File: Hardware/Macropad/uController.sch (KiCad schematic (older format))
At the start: 17 parts, among them J1 Conn_02x03_Odd_Even, SW11 SW_Push, U1 ATmega32U4-AU, X1 KC2016K

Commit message: Schematic mostly done. Started grouping components in layout
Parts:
- gave numbers to parts that had none: 3
- renumbered C13 to C32, C12 to C33, C14 to C34, C15 to C35, C16 to C36, J1 to J3, R6 to R17, R7 to R18, SW11 to SW22, U1 to U5
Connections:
- net USBD_N renamed DM1_N
- net USBD_P renamed DP1_P

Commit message: First pass of the layout done
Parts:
- removed R17: 4K7, resistor_smd:R_0603_1608Metric, symbol Device:R
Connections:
- net +3V3: now also X1.1 (EN)
- net COL[0]: now also U5.8 (PB0); no longer U5.1 (PE6)
- net COL[1]: now also U5.12 (PB7); no longer U5.40 (PF1)
- net COL[2]: now also U5.18 (PD0); no longer U5.41 (PF0)
- net COL[3]: now also U5.28 (PB4); no longer U5.27 (PD7)
- net RGB_OUT: now also U5.40 (PF1); no longer U5.18 (PD0)
- net ROT_ENC_A: now also U5.31 (PC6); no longer U5.29 (PB5)
- net ROT_ENC_B: now also U5.32 (PC7); no longer U5.30 (PB6)
- net ROW[0]: now also U5.25 (PD4); no longer U5.39 (PF4)
- net ROW[1]: now also U5.22 (PD5); no longer U5.38 (PF5)
- net ROW[2]: now also U5.21 (PD3); no longer U5.37 (PF6)
- net ROW[3]: now also U5.20 (PD2); no longer U5.36 (PF7)
- net ROW[4]: now also U5.19 (PD1); no longer U5.31 (PC6)
- net ROW[5]: now also U5.27 (PD7); no longer U5.32 (PC7)
- net SCL: now also U5.1 (PE6); no longer U5.20 (PD2)
- net SDA: now also U5.41 (PF0); no longer U5.19 (PD1)
- net DM1_N renamed USB_D4-
- net DP1_P renamed USB_D4+
- no-connect marks 5 -> 1
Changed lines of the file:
@@
 Wire Wire Line
 	5000 6250 5000 6300
-Text GLabel 5950 5500 2    50   Input ~ 0
+Text GLabel 5950 4500 2    50   Input ~ 0
 ROW[0]
-Text GLabel 5950 5600 2    50   Input ~ 0
+Text GLabel 5950 4600 2    50   Input ~ 0
 ROW[1]
-Text GLabel 5950 5700 2    50   Input ~ 0
+Text GLabel 5950 4400 2    50   Input ~ 0
 ROW[2]
-Text GLabel 5950 5400 2    50   Output ~ 0
-COL[1]
-Text GLabel 5950 5300 2    50   Output ~ 0
-COL[2]
-Wire Wire Line
-	5600 5700 5950 5700
-Wire Wire Line
-	5600 5500 5950 5500
-Wire Wire Line
-	5600 5300 5950 5300
-Wire Wire Line
-	5600 5400 5950 5400
+Wire Wire Line
+	5600 4400 5950 4400
+Wire Wire Line
+	5600 4500 5950 4500
+Wire Wire Line
+	5600 4100 5950 4100
 $Comp
 L Device:C C?
@@
 Wire Wire Line
 	4200 2525 4200 2450
-Text GLabel 5950 3400 2    50   Input ~ 0
-ROT_ENC_A
-Text GLabel 5950 3500 2    50   Input ~ 0
-ROT_ENC_B
-Wire Wire Line
-	5600 3400 5950 3400
-Wire Wire Line
-	5600 3500 5950 3500
+Wire Wire Line
+	5600 3800 5950 3800
+Wire Wire Line
+	5600 3900 5950 3900
 Text Notes 750  1000 0    197  ~ 0
 uController
 NoConn ~ 4400 3300
-$Comp
-L Device:R R?
-U 1 1 60D6928E
-P 2775 3050
-AR Path="/60D6928E" Ref="R?"  Part="1"
-AR Path="/60D44BDB/60D6928E" Ref="R?"  Part="1"
-AR Path="/62022D96/60D6928E" Ref="R17"  Part="1"
-F 0 "R17" V 2700 3050 50  0000 C CNN
-F 1 "4K7" V 2775 3050 50  0000 C CNN
-F 2 "resistor_smd:R_0603_1608Metric" V 2705 3050 50  0001 C CNN
-F 3 "~" H 2775 3050 50  0001 C CNN
-	1    2775 3050
-	1    0    0    1
-$EndComp
 Wire Wire Line
 	2950 3100 2950 3050
 Wire Wire Line
 	3675 3300 3675 3250
-Wire Wire Line
-	2775 2850 2775 2900
 Wire Wire Line
 	3650 3100 4400 3100
@@
 Wire Notes Line
 	7250 3650 8875 3650
-Text GLabel 5950 5100 2    50   Output ~ 0
-COL[0]
-Wire Wire Line
-	5600 5600 5950 5600
+Wire Wire Line
+	5600 4600 5950 4600
 $Comp
 L power:VBUS #PWR?
@@
 	1    0    0    -1
 $EndComp
-NoConn ~ 5600 3300
-NoConn ~ 5600 4500
-NoConn ~ 5600 4600
-NoConn ~ 5600 4700
 Wire Wire Line
 	8400 4400 8400 4300
@@
 Wire Wire Line
 	4250 3400 4250 3500
-$Comp
-L power:+3.3V #PWR?
-U 1 1 60D692E9
-P 2775 2850
-AR Path="/60D692E9" Ref="#PWR?"  Part="1"
-AR Path="/60D44BDB/60D692E9" Ref="#PWR?"  Part="1"
-AR Path="/62022D96/60D692E9" Ref="#PWR0149"  Part="1"
-F 0 "#PWR0149" H 2775 2700 50  0001 C CNN
-F 1 "+3.3V" H 2790 3023 50  0000 C CNN
-F 2 "" H 2775 2850 50  0001 C CNN
-F 3 "" H 2775 2850 50  0001 C CNN
-	1    2775 2850
-	1    0    0    -1
-$EndComp
 $Comp
 L power:+3.3V #PWR?
@@
 	3650 3250 3675 3250
 Wire Wire Line
-	2775 3200 2775 3250
-Wire Wire Line
-	2775 3250 3000 3250
-Wire Wire Line
 	3000 3100 2950 3100
-Wire Wire Line
-	5950 5100 5600 5100
 $Comp
 L Switch:SW_Push SW22
@@
 Wire Notes Line
 	8875 5075 8875 3650
-Text GLabel 5950 3800 2    50   Input ~ 0
+Text GLabel 5950 4200 2    50   Input ~ 0
 ROW[4]
 Wire Wire Line
-	5950 3800 5600 3800
-Text GLabel 5950 4100 2    50   Output ~ 0
+	5950 4200 5600 4200
+Text GLabel 5950 5400 2    50   Output ~ 0
 RGB_OUT
 Wire Wire Line
-	5950 4100 5600 4100
+	5950 5400 5600 5400
 Text Notes 2750 2525 0    50   ~ 0
 16MHz Crystal
@@
 Wire Notes Line
 	10125 6000 8950 6000
-Text GLabel 5950 5800 2    50   Input ~ 0
+Text GLabel 5950 4300 2    50   Input ~ 0
 ROW[3]
 Wire Wire Line
-	5600 5800 5950 5800
+	5600 4300 5950 4300
 $Comp
 L Device:R R?
@@
 Wire Wire Line
 	6450 5000 6450 5075
-Text GLabel 5950 3900 2    50   Input ~ 0
+Text GLabel 5950 4800 2    50   Input ~ 0
 ROW[5]
 Wire Wire Line
-	5950 3900 5600 3900
-Text GLabel 5950 4800 2    50   Output ~ 0
-COL[3]
-Wire Wire Line
 	5950 4800 5600 4800
-Text GLabel 5950 4200 2    50   BiDi ~ 0
+Wire Wire Line
+	5950 3300 5600 3300
+Text GLabel 5950 5300 2    50   BiDi ~ 0
 SDA
 Wire Wire Line
-	5950 4200 5600 4200
-Text GLabel 5950 4300 2    50   BiDi ~ 0
+	5950 5300 5600 5300
+Text GLabel 5950 5100 2    50   BiDi ~ 0
 SCL
 Wire Wire Line
-	5950 4300 5600 4300
+	5950 5100 5600 5100
 $Comp
 L Device:R R?
@@
 Wire Wire Line
 	3925 4000 4400 4000
-Text GLabel 3925 3900 0    50   BiDi ~ 0
-DP1_P
-Text GLabel 3925 4000 0    50   BiDi ~ 0
-DM1_N
 Text GLabel 8000 3250 2    50   BiDi ~ 0
 SDA
+Wire Wire Line
+	3000 3250 2950 3250
+Wire Wire Line
+	2950 3250 2950 3100
+Connection ~ 2950 3100
+Wire Wire Line
+	5600 3600 5950 3600
+Text GLabel 5950 4100 2    50   Output ~ 0
+COL[2]
+Wire Wire Line
+	5950 2900 5600 2900
+Text GLabel 5950 2900 2    50   Output ~ 0
+COL[0]
+Text GLabel 5950 3600 2    50   Output ~ 0
+COL[1]
+Text GLabel 5950 3900 2    50   Input ~ 0
+ROT_ENC_B
+Text GLabel 5950 3800 2    50   Input ~ 0
+ROT_ENC_A
+Text GLabel 5950 3300 2    50   Output ~ 0
+COL[3]
+Text GLabel 3925 3900 0    50   BiDi ~ 0
+USB_D4+
+Text GLabel 3925 4000 0    50   BiDi ~ 0
+USB_D4-
 $EndSCHEMATC

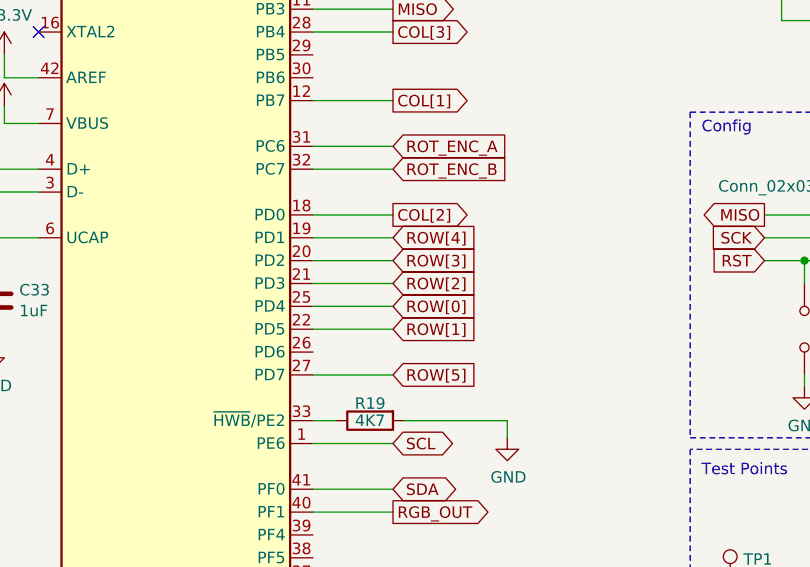
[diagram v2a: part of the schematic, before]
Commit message: Redoing layout with key switches upside down for better LED placement
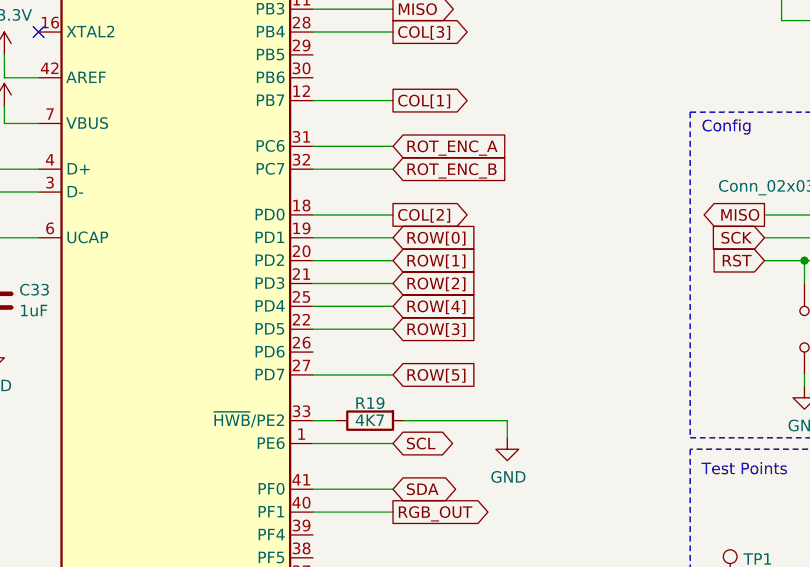
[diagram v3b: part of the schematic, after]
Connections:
- net ROW[0]: now also U5.19 (PD1); no longer U5.25 (PD4)
- net ROW[1]: now also U5.20 (PD2); no longer U5.22 (PD5)
- net ROW[3]: now also U5.22 (PD5); no longer U5.20 (PD2)
- net ROW[4]: now also U5.25 (PD4); no longer U5.19 (PD1)
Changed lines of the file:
@@
 Wire Wire Line
 	5000 6250 5000 6300
-Text GLabel 5950 4500 2    50   Input ~ 0
+Text GLabel 5950 4200 2    50   Input ~ 0
 ROW[0]
-Text GLabel 5950 4600 2    50   Input ~ 0
+Text GLabel 5950 4300 2    50   Input ~ 0
 ROW[1]
 Text GLabel 5950 4400 2    50   Input ~ 0
@@
 	5600 4400 5950 4400
 Wire Wire Line
-	5600 4500 5950 4500
+	5600 4200 5950 4200
 Wire Wire Line
 	5600 4100 5950 4100
@@
 	7250 3650 8875 3650
 Wire Wire Line
-	5600 4600 5950 4600
+	5600 4300 5950 4300
 $Comp
 L power:VBUS #PWR?
@@
 Wire Notes Line
 	8875 5075 8875 3650
-Text GLabel 5950 4200 2    50   Input ~ 0
+Text GLabel 5950 4500 2    50   Input ~ 0
 ROW[4]
 Wire Wire Line
-	5950 4200 5600 4200
+	5950 4500 5600 4500
 Text GLabel 5950 5400 2    50   Output ~ 0
 RGB_OUT
@@
 Wire Notes Line
 	10125 6000 8950 6000
-Text GLabel 5950 4300 2    50   Input ~ 0
-ROW[3]
-Wire Wire Line
-	5600 4300 5950 4300
 $Comp
 L Device:R R?
@@
 Text GLabel 3925 4000 0    50   BiDi ~ 0
 USB_D4-
+Wire Wire Line
+	5600 4600 5950 4600
+Text GLabel 5950 4600 2    50   Input ~ 0
+ROW[3]
 $EndSCHEMATC

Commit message: Layout done, cleaned up schematic and generated gerbers
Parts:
- removed R20, R21: 4K7, resistor_smd:R_0603_1608Metric, symbol Device:R
- SW22: footprint button_switch_smd:SW_SPST_B3U-1000P -> custom_footprint_library:SW_SPST_B3U-1000P
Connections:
- no-connect marks 1 -> 8
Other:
- moved on the sheet: C32, C33, C34, C35, C36, J3, R18, R19, SW22, TP1, TP2, TP3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
